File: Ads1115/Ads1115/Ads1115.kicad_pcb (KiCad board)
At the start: 2 copper layers, 1 part, among them U1 ADS1115IDGS

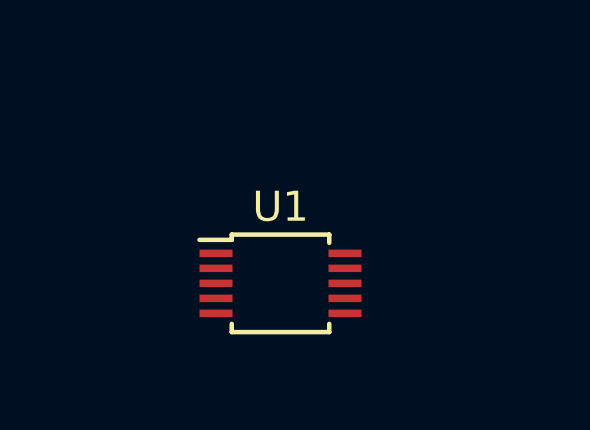
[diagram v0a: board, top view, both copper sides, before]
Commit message: add ads1111 and ads1248
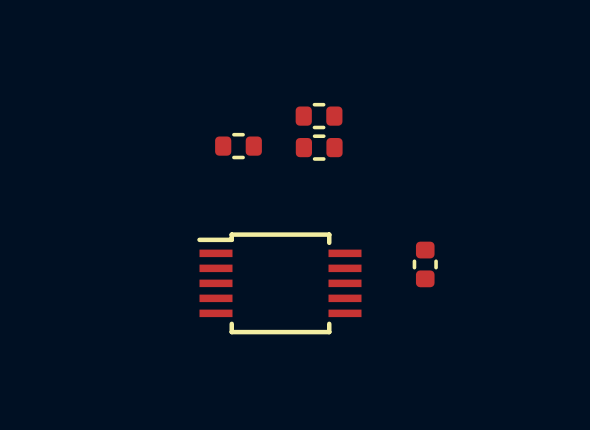
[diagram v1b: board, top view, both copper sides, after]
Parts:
- added ADC_Alert_R1: 10k, Resistor_SMD:R_0402_1005Metric, F.Cu at (132.4, 88.0)
- added ADC_C1: 0.1uF, Capacitor_SMD:C_0402_1005Metric, F.Cu at (138.7, 91.9)
- added ADC_SCL_R1: 10k, Resistor_SMD:R_0402_1005Metric, F.Cu at (135.1, 88.0)
- added ADC_SDA_R1: 10k, Resistor_SMD:R_0402_1005Metric, F.Cu at (135.1, 87.0)
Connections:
- U1 pad 1: unconnected-(U1-ADDR-Pad1) -> GND
- U1 pad 10: unconnected-(U1-SCL-Pad10) -> /SCL
- U1 pad 2: unconnected-(U1-ALERT/RDY-Pad2) -> /Alert
- U1 pad 3: unconnected-(U1-GND-Pad3) -> GND
- U1 pad 8: unconnected-(U1-VDD-Pad8) -> +5V
- U1 pad 9: unconnected-(U1-SDA-Pad9) -> /SDA

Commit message: updates ads1115 and ads 1248
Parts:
- removed U1: ADS1115IDGS, Package_SO:TSSOP-10_3x3mm_P0.5mm
- added ADC_C2: 0.1uF, Capacitor_SMD:C_0402_1005Metric, F.Cu at (129.4, 92.3)
- added ADC_C3: 0.1uF, Capacitor_SMD:C_0402_1005Metric, F.Cu at (129.4, 94.2)
- added ADC_C4: 0.1uF, Capacitor_SMD:C_0402_1005Metric, F.Cu at (138.6, 94.3)
- added ADC_C5: 0.1uF, Capacitor_SMD:C_0402_1005Metric, F.Cu at (138.6, 92.5)
- added ADC_C6: 0.1uF, Capacitor_SMD:C_0402_1005Metric, F.Cu at (130.3, 93.3)
- added ADC_C7: 0.1uF, Capacitor_SMD:C_0402_1005Metric, F.Cu at (137.6, 93.4)
- added ADS1115_U1: ADS1115IDGS, Package_SO:TSSOP-10_3x3mm_P0.5mm, F.Cu at (133.9, 92.6)
- moved ADC_SDA_R1 3.14 mm to (135.4, 90.1), turned to 0 degrees
- moved ADC_SCL_R1 3.02 mm to (137.7, 89.7), turned to 180 degrees
- moved ADC_Alert_R1 2.13 mm to (132.5, 90.1), turned to 0 degrees
- moved ADC_C1 1.01 mm to (138.7, 90.9), turned to 180 degrees
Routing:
- net +5V: track 0.00 -> 13.7 mm, vias 0 -> 3
- net /Alert: track 0.00 -> 4.77 mm
- net /SDA: track 0.00 -> 4.66 mm
- net A3: track 0.00 -> 4.28 mm
- net A2: track 0.00 -> 4.28 mm
- net GND: track 0.00 -> 4.20 mm
- net /SCL: track 0.00 -> 3.99 mm
- net A0: track 0.00 -> 3.80 mm
- net A1: track 0.00 -> 3.75 mm
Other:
- board text added: "ADDR"
- board text added: "ANI0"
- board text added: "ANI1"
- board text added: "ANI2"
- board text added: "ANI3"
- board text added: "Alert"
- board text added: "SCL"
- board text added: "SDA"
